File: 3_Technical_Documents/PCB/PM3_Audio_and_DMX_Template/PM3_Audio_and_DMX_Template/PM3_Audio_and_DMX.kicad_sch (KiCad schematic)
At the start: 10 parts, among them J1 DMX-out

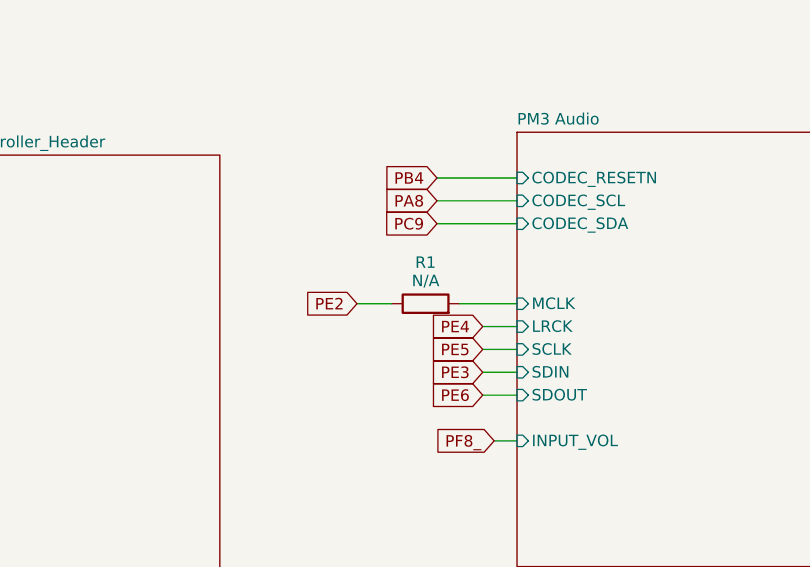
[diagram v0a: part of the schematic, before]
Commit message: codec and layout
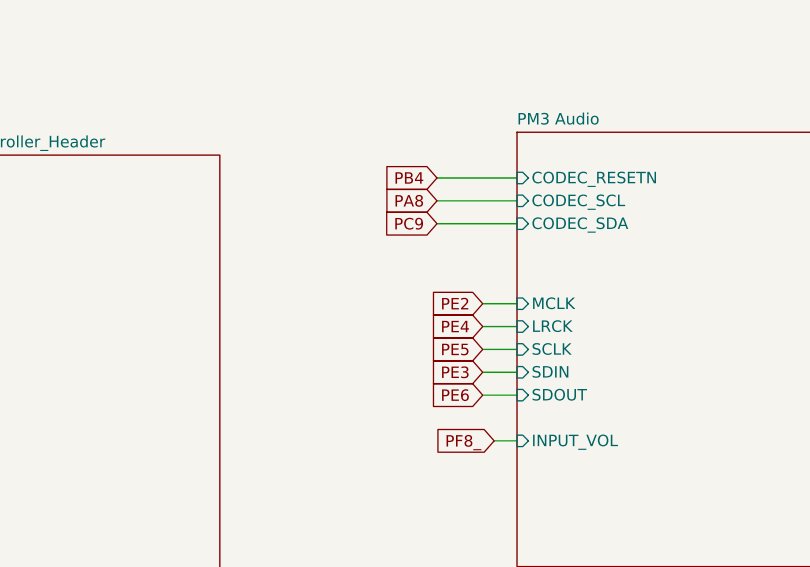
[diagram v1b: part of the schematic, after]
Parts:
- removed R1: N/A, Resistor_SMD:R_0603_1608Metric, symbol Device:R
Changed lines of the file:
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@@
 	(wire
 		(pts
-			(xy 85.09 54.61) (xy 91.44 54.61)
+			(xy 82.55 143.51) (xy 82.55 146.05)
 		)
 		(stroke
@@
 	(wire
 		(pts
-			(xy 82.55 143.51) (xy 82.55 146.05)
+			(xy 50.8 138.43) (xy 52.07 138.43)
 		)
 		(stroke
@@
 	(wire
 		(pts
-			(xy 50.8 138.43) (xy 52.07 138.43)
+			(xy 82.55 43.18) (xy 91.44 43.18)
 		)
 		(stroke
@@
 	(wire
 		(pts
-			(xy 82.55 43.18) (xy 91.44 43.18)
+			(xy 87.63 54.61) (xy 91.44 54.61)
 		)
 		(stroke
@@
 	(wire
 		(pts
-			(xy 73.66 54.61) (xy 77.47 54.61)
+			(xy 259.08 113.03) (xy 259.08 114.3)
 		)
 		(stroke
@@
 	(wire
 		(pts
-			(xy 259.08 113.03) (xy 259.08 114.3)
+			(xy 82.55 45.72) (xy 91.44 45.72)
 		)
 		(stroke
@@
 	(wire
 		(pts
-			(xy 82.55 45.72) (xy 91.44 45.72)
+			(xy 88.9 69.85) (xy 91.44 69.85)
 		)
 		(stroke
@@
 	(wire
 		(pts
-			(xy 88.9 69.85) (xy 91.44 69.85)
+			(xy 227.33 97.79) (xy 259.08 97.79)
 		)
 		(stroke
@@
 	(wire
 		(pts
-			(xy 227.33 97.79) (xy 259.08 97.79)
+			(xy 87.63 57.15) (xy 91.44 57.15)
 		)
 		(stroke
@@
 	(wire
 		(pts
-			(xy 87.63 57.15) (xy 91.44 57.15)
+			(xy 227.33 105.41) (xy 251.46 105.41)
 		)
 		(stroke
@@
 		)
 	)
-	(wire
-		(pts
-			(xy 227.33 105.41) (xy 251.46 105.41)
-		)
-		(stroke
-			(width 0)
-			(type default)
-		)
-	)
 	(global_label "PE5"
 		(shape input)
@@
 	(global_label "PE2"
 		(shape input)
-		(at 73.66 54.61 180)
+		(at 87.63 54.61 180)
 		(fields_autoplaced yes)
 		(effects
@@
 		)
 		(property "Intersheetrefs" "${INTERSHEET_REFS}"
-			(at 67.0463 54.61 0)
+			(at 81.0163 54.61 0)
 			(effects
 				(font
@@
 					(unit 1)
 				)
-			)
-		)
-	)
-	(symbol
-		(lib_id "Device:R")
-		(at 81.28 54.61 90)
-		(unit 1)
-		(exclude_from_sim no)
-		(in_bom yes)
-		(on_board yes)
-		(dnp no)
-		(property "Reference" "R1"
-			(at 81.28 50.038 90)
-			(effects
-				(font
-					(size 1.27 1.27)
-				)
-			)
-		)
-		(property "Value" "N/A"
-			(at 81.28 52.07 90)
-			(effects
-				(font
-					(size 1.27 1.27)
-				)
-			)
-		)
-		(property "Footprint" "Resistor_SMD:R_0603_1608Metric"
-			(at 81.28 56.388 90)
-			(effects
-				(font
-					(size 1.27 1.27)
-				)
-				(hide yes)
-			)
-		)
-		(property "Datasheet" "~"
-			(at 81.28 54.61 0)
-			(effects
-				(font
-					(size 1.27 1.27)
-				)
-				(hide yes)
-			)
-		)
-		(property "Description" "Resistor"
-			(at 81.28 54.61 0)
-			(effects
-				(font
-					(size 1.27 1.27)
-				)
-				(hide yes)
-			)
-		)
-		(property "MPN" ""
-			(at 81.28 54.61 90)
-			(effects
-				(font
-					(size 1.27 1.27)
-				)
-				(hide yes)
-			)
-		)
-		(property "Manufacturer" ""
-			(at 81.28 54.61 90)
-			(effects
-				(font
-					(size 1.27 1.27)
-				)
-				(hide yes)
-			)
-		)
-		(pin "1"
-		)
-		(pin "2"
-		)
-		(instances
-			(project ""
-				(path "/1f276d59-ad9b-4e70-a842-f3b7e562eb9b"
-					(reference "R1")
-					(unit 1)
-				)

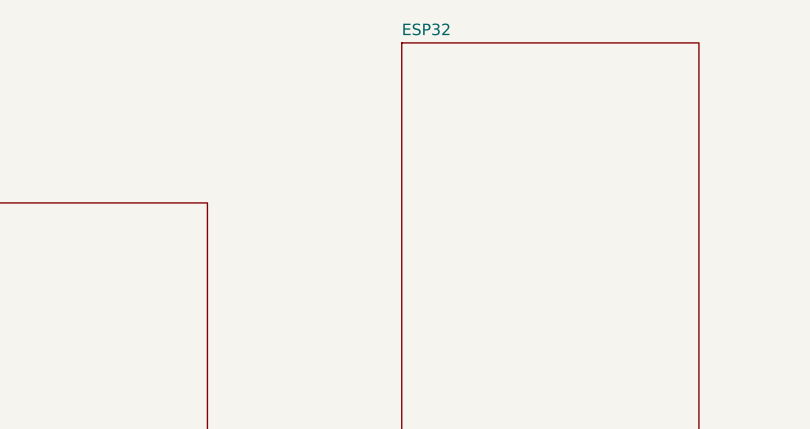
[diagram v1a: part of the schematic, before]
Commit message: i2s added
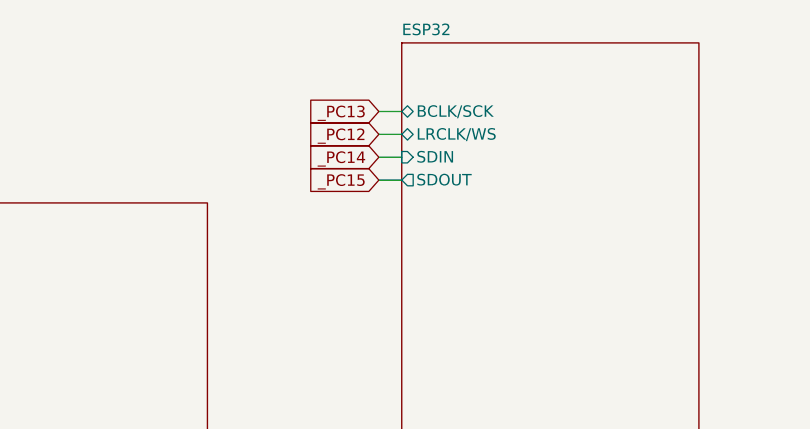
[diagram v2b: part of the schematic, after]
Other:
- sheet ESP32 ports: added BCLK/SCK, LRCLK/WS, SDIN, SDOUT; removed none
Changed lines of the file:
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@@
+	(wire
+		(pts
+			(xy 168.91 27.94) (xy 171.45 27.94)
+		)
+		(stroke
+			(width 0)
+			(type default)
+		)
+	)
 	(wire
 		(pts
@@
 	(wire
 		(pts
+			(xy 168.91 30.48) (xy 171.45 30.48)
+		)
+		(stroke
+			(width 0)
+			(type default)
+		)
+	)
+	(wire
+		(pts
 			(xy 74.93 143.51) (xy 74.93 146.05)
 		)
@@
 	(wire
 		(pts
+			(xy 168.91 33.02) (xy 171.45 33.02)
+		)
+		(stroke
+			(width 0)
+			(type default)
+		)
+	)
+	(wire
+		(pts
 			(xy 74.93 146.05) (xy 82.55 146.05)
 		)
@@
 	(wire
 		(pts
+			(xy 168.91 25.4) (xy 171.45 25.4)
+		)
+		(stroke
+			(width 0)
+			(type default)
+		)
+	)
+	(wire
+		(pts
 			(xy 82.55 43.18) (xy 91.44 43.18)
 		)
@@
 			(width 0)
 			(type default)
+		)
+	)
+	(global_label "_PC12"
+		(shape input)
+		(at 168.91 27.94 180)
+		(fields_autoplaced yes)
+		(effects
+			(font
+				(size 1.27 1.27)
+			)
+			(justify right)
+		)
+		(property "Intersheetrefs" "${INTERSHEET_REFS}"
+			(at 159.9982 27.94 0)
+			(effects
+				(font
+					(size 1.27 1.27)
+				)
+				(justify right)
+				(hide yes)
+			)
+		)
+	)
+	(global_label "_PC13"
+		(shape input)
+		(at 168.91 25.4 180)
+		(fields_autoplaced yes)
+		(effects
+			(font
+				(size 1.27 1.27)
+			)
+			(justify right)
+		)
+		(property "Intersheetrefs" "${INTERSHEET_REFS}"
+			(at 159.9982 25.4 0)
+			(effects
+				(font
+					(size 1.27 1.27)
+				)
+				(justify right)
+				(hide yes)
+			)
 		)
 	)
@@
 		)
 	)
+	(global_label "_PC14"
+		(shape input)
+		(at 168.91 30.48 180)
+		(fields_autoplaced yes)
+		(effects
+			(font
+				(size 1.27 1.27)
+			)
+			(justify right)
+		)
+		(property "Intersheetrefs" "${INTERSHEET_REFS}"
+			(at 159.9982 30.48 0)
+			(effects
+				(font
+					(size 1.27 1.27)
+				)
+				(justify right)
+				(hide yes)
+			)
+		)
+	)
 	(global_label "PE4"
 		(shape input)
@@
 		(property "Intersheetrefs" "${INTERSHEET_REFS}"
 			(at 182.5558 97.79 0)
+			(effects
+				(font
+					(size 1.27 1.27)
+				)
+				(justify right)
+				(hide yes)
+			)
+		)
+	)
+	(global_label "_PC15"
+		(shape input)
+		(at 168.91 33.02 180)
+		(fields_autoplaced yes)
+		(effects
+			(font
+				(size 1.27 1.27)
+			)
+			(justify right)
+		)
+		(property "Intersheetrefs" "${INTERSHEET_REFS}"
+			(at 159.9982 33.02 0)
 			(effects
 				(font
@@
 			)
 		)
+		(pin "BCLK{slash}SCK" bidirectional
+			(at 171.45 25.4 180)
+			(effects
+				(font
+					(size 1.27 1.27)
+				)
+				(justify left)
+			)
+		)
+		(pin "LRCLK{slash}WS" bidirectional
+			(at 171.45 27.94 180)
+			(effects
+				(font
+					(size 1.27 1.27)
+				)
+				(justify left)
+			)
+		)
+		(pin "SDIN" input
+			(at 171.45 30.48 180)
+			(effects
+				(font
+					(size 1.27 1.27)
+				)
+				(justify left)
+			)
+		)
+		(pin "SDOUT" output
+			(at 171.45 33.02 180)
+			(effects
+				(font
+					(size 1.27 1.27)
+				)
+				(justify left)
+			)
+		)

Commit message: esp-stm connection (+ conflict recolution)
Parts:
- added JP11, JP12: SolderJumper_2_Open, Jumper:SolderJumper-2_P1.3mm_Open_RoundedPad1.0x1.5mm, symbol Jumper:SolderJumper_2_Open
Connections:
- net PE4: now also JP11.2 (B)
- net PE5: now also JP12.2 (B)
- new net _PB12: JP11.1 (A)
- new net _PB13: JP12.1 (A)
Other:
- sheet ESP32 ports: added BCLK/SCK_1, BCLK/SCK_2, LRCLK/WS_1, LRCLK/WS_2, MCLK, SDIN_1, SDIN_2, SDOUT_1, SDOUT_2, UART_RX, UART_TX; removed BCLK/SCK, LRCLK/WS, SDIN, SDOUT

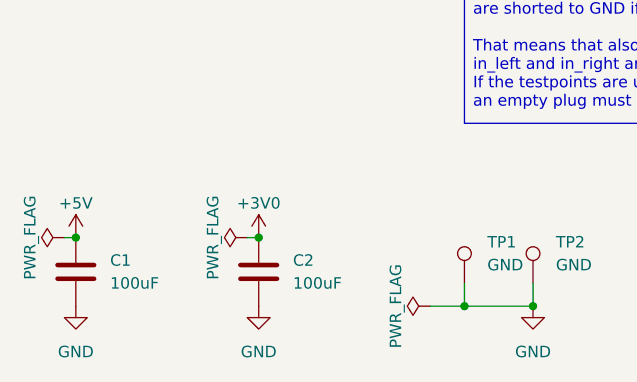
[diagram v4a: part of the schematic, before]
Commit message: schematics, layout and bom updated (to match corrections)
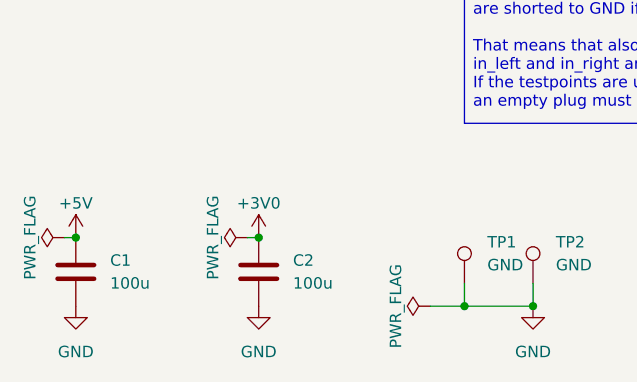
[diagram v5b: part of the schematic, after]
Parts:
- C1, C2: value 100uF -> 100u
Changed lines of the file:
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@@
 			)
 		)
-		(property "Value" "100uF"
+		(property "Value" "100u"
 			(at 55.88 143.5099 0)
 			(effects
@@
 			)
 		)
-		(property "Value" "100uF"
+		(property "Value" "100u"
 			(at 35.56 143.5099 0)
 			(effects
